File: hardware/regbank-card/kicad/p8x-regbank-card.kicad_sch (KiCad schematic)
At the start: 0 parts

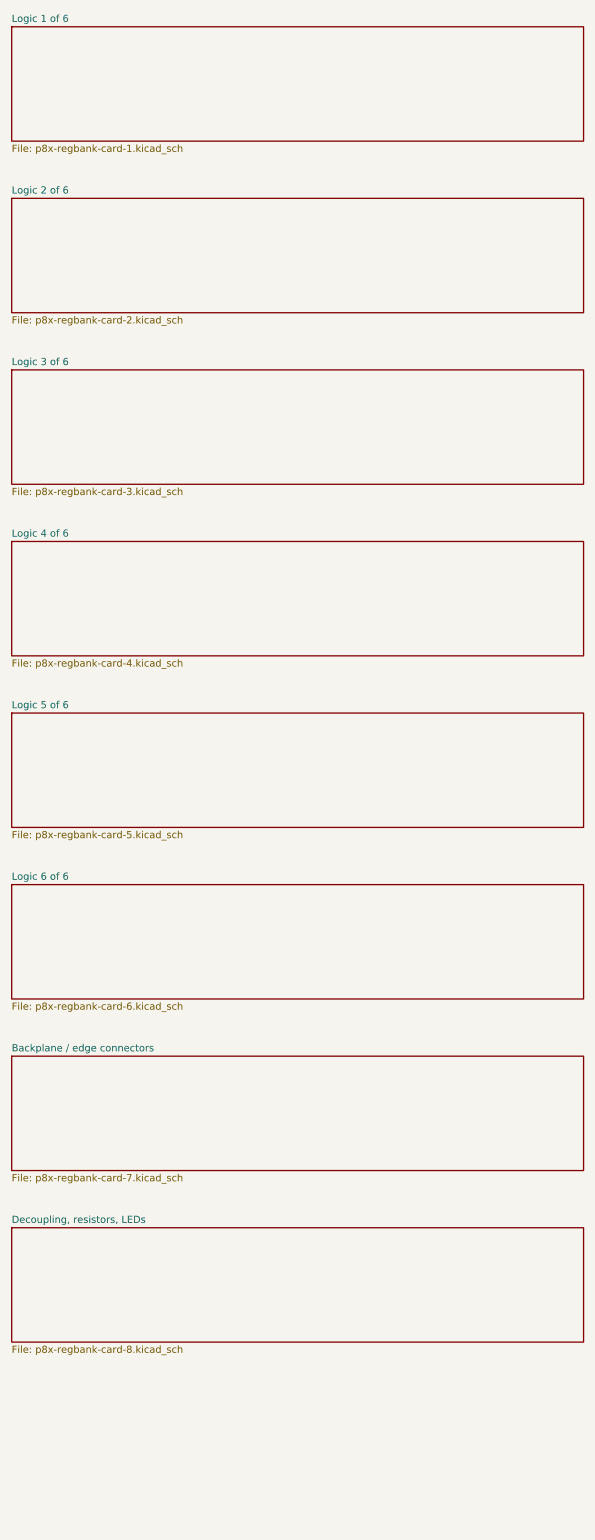
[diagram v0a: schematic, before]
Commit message: feat(sch): draw every P8X card schematic by function
Extend the functional-sheet grouping from the io-card to the control,
regbank, alu, memory, cf, ps2 and bustest cards. functional_sheets now
attaches unnamed glue gates, LEDs, resistors and connectors to the block
they share the most local nets with, so each block lists only its main
parts. A net with two or more pins on a sheet is now wired there even if
it continues elsewhere (its global name label rides on the wire), and
every wire is oriented by drawing side. The regbank gets one pointer per
sheet; the ps2 latches share a sheet with the AVR so the mailbox bus is
drawn. The bustest probe resistors use a straight-order RNISO8DSTR
drawing (the reversed B side forced every wire to cross and the sheet
fell back to labels). build_sch.sh now shows ELK fallbacks and clears old
numbered sheets before a build. All eight netlists match the boards,
ERC 0 errors; the boards change only in footprint link paths.

Co-Authored-By: Claude Opus 5.5 <noreply@anthropic.com>
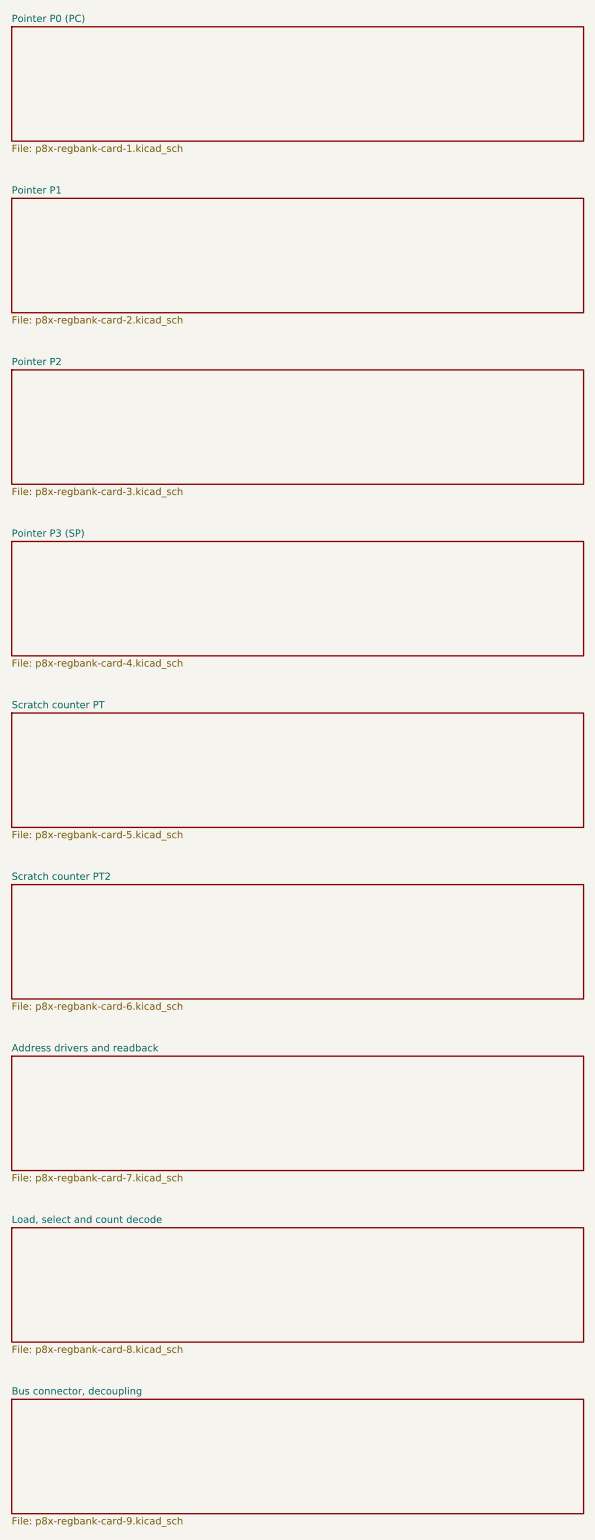
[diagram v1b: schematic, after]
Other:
- sheet Backplane / edge connectors renamed Address drivers and readback
- sheet Decoupling, resistors, LEDs renamed Load, select and count decode
- sheet Logic 1 of 6 renamed Pointer P0 (PC)
- sheet Logic 2 of 6 renamed Pointer P1
- sheet Logic 3 of 6 renamed Pointer P2
- sheet Logic 4 of 6 renamed Pointer P3 (SP)
- sheet Logic 5 of 6 renamed Scratch counter PT
- sheet Logic 6 of 6 renamed Scratch counter PT2
- added sheet Bus connector, decoupling (p8x-regbank-card-9.kicad_sch)
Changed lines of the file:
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@@
   (sheet (at 25.40 30.48) (size 101.6 20.32) (fields_autoplaced yes)
     (stroke (width 0.1524) (type solid)) (fill (color 0 0 0 0.0000))
-    (property "Sheetname" "Logic 1 of 6" (at 25.40 29.78 0) (effects (font (size 1.27 1.27)) (justify left bottom)))
+    (property "Sheetname" "Pointer P0 (PC)" (at 25.40 29.78 0) (effects (font (size 1.27 1.27)) (justify left bottom)))
     (property "Sheetfile" "p8x-regbank-card-1.kicad_sch" (at 25.40 51.38 0) (effects (font (size 1.27 1.27)) (justify left top)))
     (instances (project "p8x-regbank-card" (path "/32562f02-66ee-5b9d-82d6-2d3b554d7ba0" (page "2"))))
@@
   (sheet (at 25.40 60.96) (size 101.6 20.32) (fields_autoplaced yes)
     (stroke (width 0.1524) (type solid)) (fill (color 0 0 0 0.0000))
-    (property "Sheetname" "Logic 2 of 6" (at 25.40 60.26 0) (effects (font (size 1.27 1.27)) (justify left bottom)))
+    (property "Sheetname" "Pointer P1" (at 25.40 60.26 0) (effects (font (size 1.27 1.27)) (justify left bottom)))
     (property "Sheetfile" "p8x-regbank-card-2.kicad_sch" (at 25.40 81.86 0) (effects (font (size 1.27 1.27)) (justify left top)))
     (instances (project "p8x-regbank-card" (path "/32562f02-66ee-5b9d-82d6-2d3b554d7ba0" (page "3"))))
@@
   (sheet (at 25.40 91.44) (size 101.6 20.32) (fields_autoplaced yes)
     (stroke (width 0.1524) (type solid)) (fill (color 0 0 0 0.0000))
-    (property "Sheetname" "Logic 3 of 6" (at 25.40 90.74 0) (effects (font (size 1.27 1.27)) (justify left bottom)))
+    (property "Sheetname" "Pointer P2" (at 25.40 90.74 0) (effects (font (size 1.27 1.27)) (justify left bottom)))
     (property "Sheetfile" "p8x-regbank-card-3.kicad_sch" (at 25.40 112.34 0) (effects (font (size 1.27 1.27)) (justify left top)))
     (instances (project "p8x-regbank-card" (path "/32562f02-66ee-5b9d-82d6-2d3b554d7ba0" (page "4"))))
@@
   (sheet (at 25.40 121.92) (size 101.6 20.32) (fields_autoplaced yes)
     (stroke (width 0.1524) (type solid)) (fill (color 0 0 0 0.0000))
-    (property "Sheetname" "Logic 4 of 6" (at 25.40 121.22 0) (effects (font (size 1.27 1.27)) (justify left bottom)))
+    (property "Sheetname" "Pointer P3 (SP)" (at 25.40 121.22 0) (effects (font (size 1.27 1.27)) (justify left bottom)))
     (property "Sheetfile" "p8x-regbank-card-4.kicad_sch" (at 25.40 142.82 0) (effects (font (size 1.27 1.27)) (justify left top)))
     (instances (project "p8x-regbank-card" (path "/32562f02-66ee-5b9d-82d6-2d3b554d7ba0" (page "5"))))
@@
   (sheet (at 25.40 152.40) (size 101.6 20.32) (fields_autoplaced yes)
     (stroke (width 0.1524) (type solid)) (fill (color 0 0 0 0.0000))
-    (property "Sheetname" "Logic 5 of 6" (at 25.40 151.70 0) (effects (font (size 1.27 1.27)) (justify left bottom)))
+    (property "Sheetname" "Scratch counter PT" (at 25.40 151.70 0) (effects (font (size 1.27 1.27)) (justify left bottom)))
     (property "Sheetfile" "p8x-regbank-card-5.kicad_sch" (at 25.40 173.30 0) (effects (font (size 1.27 1.27)) (justify left top)))
     (instances (project "p8x-regbank-card" (path "/32562f02-66ee-5b9d-82d6-2d3b554d7ba0" (page "6"))))
@@
   (sheet (at 25.40 182.88) (size 101.6 20.32) (fields_autoplaced yes)
     (stroke (width 0.1524) (type solid)) (fill (color 0 0 0 0.0000))
-    (property "Sheetname" "Logic 6 of 6" (at 25.40 182.18 0) (effects (font (size 1.27 1.27)) (justify left bottom)))
+    (property "Sheetname" "Scratch counter PT2" (at 25.40 182.18 0) (effects (font (size 1.27 1.27)) (justify left bottom)))
     (property "Sheetfile" "p8x-regbank-card-6.kicad_sch" (at 25.40 203.78 0) (effects (font (size 1.27 1.27)) (justify left top)))
     (instances (project "p8x-regbank-card" (path "/32562f02-66ee-5b9d-82d6-2d3b554d7ba0" (page "7"))))
@@
   (sheet (at 25.40 213.36) (size 101.6 20.32) (fields_autoplaced yes)
     (stroke (width 0.1524) (type solid)) (fill (color 0 0 0 0.0000))
-    (property "Sheetname" "Backplane / edge connectors" (at 25.40 212.66 0) (effects (font (size 1.27 1.27)) (justify left bottom)))
+    (property "Sheetname" "Address drivers and readback" (at 25.40 212.66 0) (effects (font (size 1.27 1.27)) (justify left bottom)))
     (property "Sheetfile" "p8x-regbank-card-7.kicad_sch" (at 25.40 234.26 0) (effects (font (size 1.27 1.27)) (justify left top)))
     (instances (project "p8x-regbank-card" (path "/32562f02-66ee-5b9d-82d6-2d3b554d7ba0" (page "8"))))
@@
   (sheet (at 25.40 243.84) (size 101.6 20.32) (fields_autoplaced yes)
     (stroke (width 0.1524) (type solid)) (fill (color 0 0 0 0.0000))
-    (property "Sheetname" "Decoupling, resistors, LEDs" (at 25.40 243.14 0) (effects (font (size 1.27 1.27)) (justify left bottom)))
+    (property "Sheetname" "Load, select and count decode" (at 25.40 243.14 0) (effects (font (size 1.27 1.27)) (justify left bottom)))
     (property "Sheetfile" "p8x-regbank-card-8.kicad_sch" (at 25.40 264.74 0) (effects (font (size 1.27 1.27)) (justify left top)))
     (instances (project "p8x-regbank-card" (path "/32562f02-66ee-5b9d-82d6-2d3b554d7ba0" (page "9"))))
   )
+  (sheet (at 25.40 274.32) (size 101.6 20.32) (fields_autoplaced yes)
+    (stroke (width 0.1524) (type solid)) (fill (color 0 0 0 0.0000))
+    (property "Sheetname" "Bus connector, decoupling" (at 25.40 273.62 0) (effects (font (size 1.27 1.27)) (justify left bottom)))
+    (property "Sheetfile" "p8x-regbank-card-9.kicad_sch" (at 25.40 295.22 0) (effects (font (size 1.27 1.27)) (justify left top)))
+    (instances (project "p8x-regbank-card" (path "/32562f02-66ee-5b9d-82d6-2d3b554d7ba0" (page "10"))))
+  )
   (sheet_instances (path "/" (page "1")))
